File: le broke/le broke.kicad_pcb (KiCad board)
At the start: 2 copper layers, 100 x 81 mm, 42 parts, among them SW1 SW_Push, U1 ProMicro

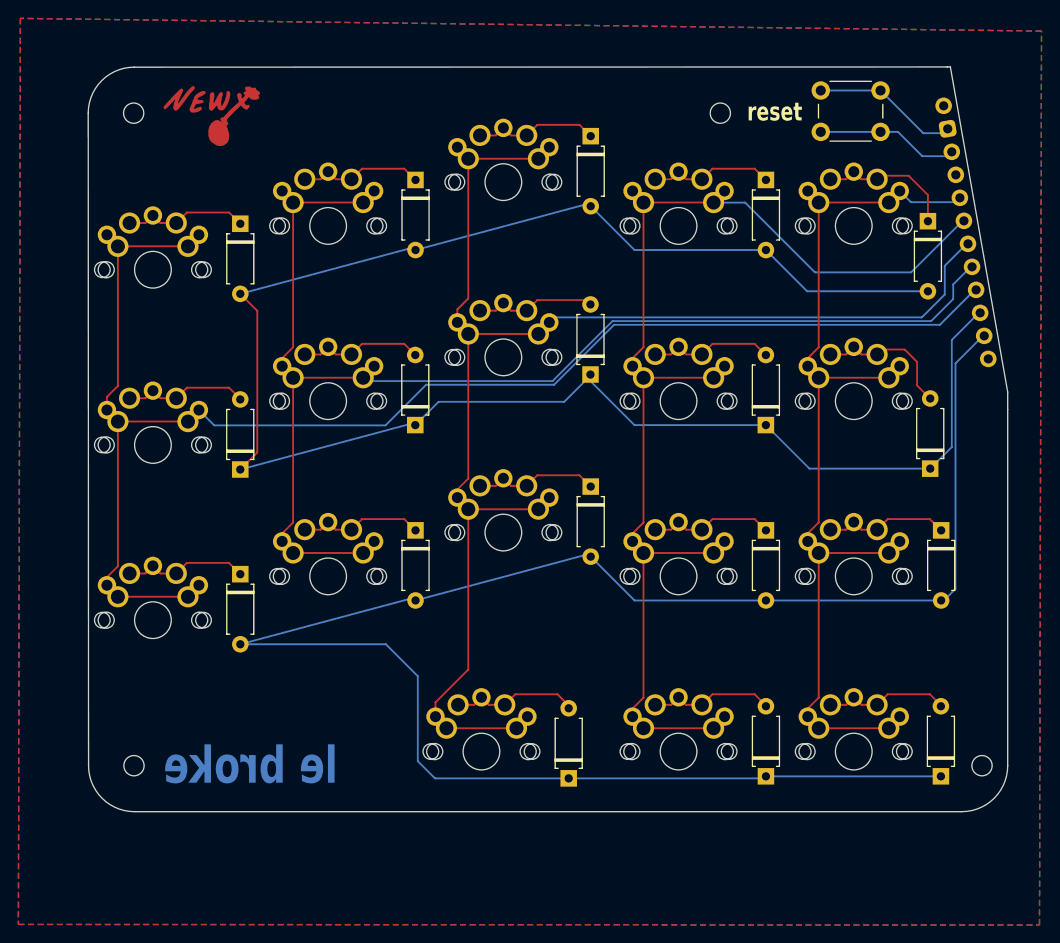
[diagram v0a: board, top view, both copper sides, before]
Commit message: added 2u spacebar support
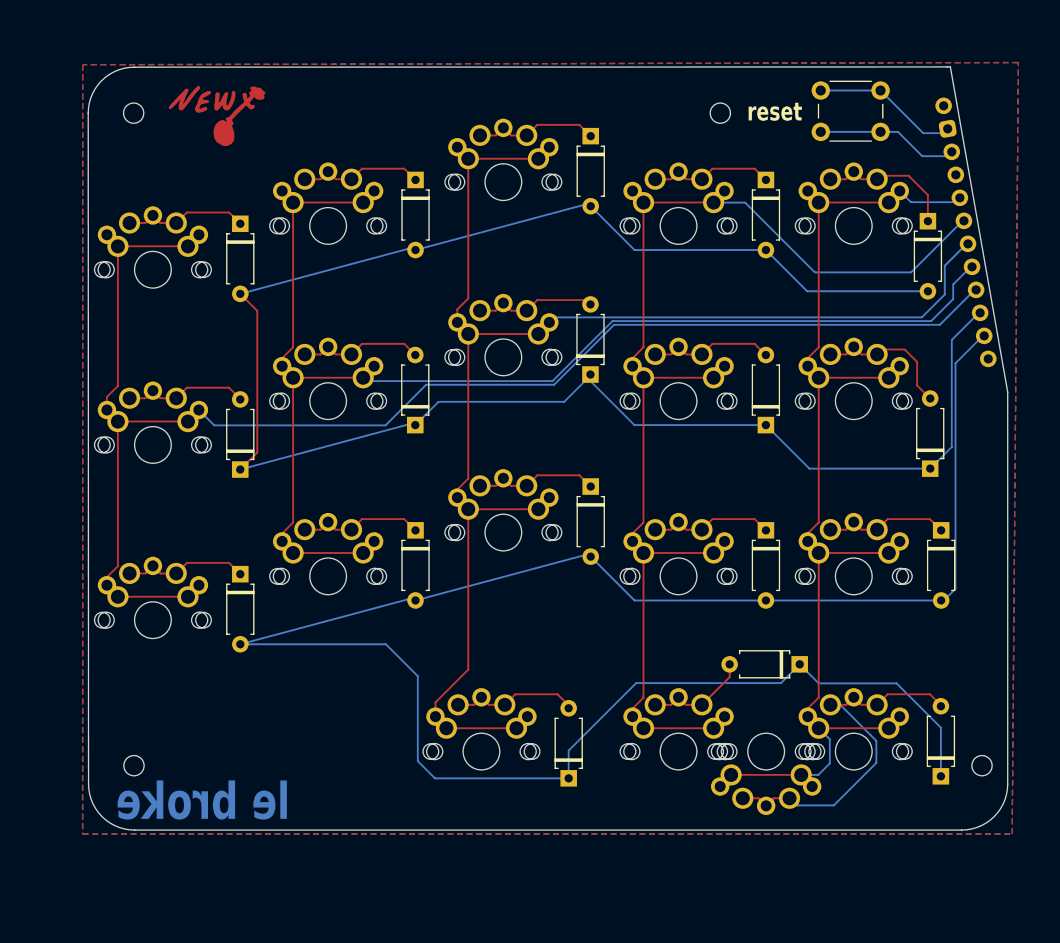
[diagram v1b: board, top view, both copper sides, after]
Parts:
- added MX18: MX_SW_solder, marbastlib-mx:SW_MX_1u_rev, F.Cu at (166.9, 125.5)
- moved D17 12.7 mm to (170.5, 116.0), turned to 180 degrees
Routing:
- net Net-(D18-A): track 13.7 -> 40.1 mm
- net ROW1: track 198.3 -> 214.1 mm
- net COL4: track 92.7 -> 108.3 mm
- net Net-(D17-A): track 13.7 -> 11.4 mm
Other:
- board size 100 x 81 mm -> 100 x 83 mm

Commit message: Updated kicad folder
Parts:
- moved REF** 28.6 mm to (108.8, 82.6)
- moved REF** 27.5 mm to (108.8, 101.6)
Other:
- board size 100 x 83 mm -> 99.9 x 83 mm
- board text added: "edge cut edit by mhzkb"
